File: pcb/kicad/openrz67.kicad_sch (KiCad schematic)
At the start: 58 parts, among them J1 GPIO header, U1 ESP32-C3FH4, U2 TPS63031DSKR, U3 BQ25185DLHR, U4 S4B-XH-A(LF)(SN), U5 TLP172AM, U6 TLP172AM, X1 40MHz, X2 32.768kHz

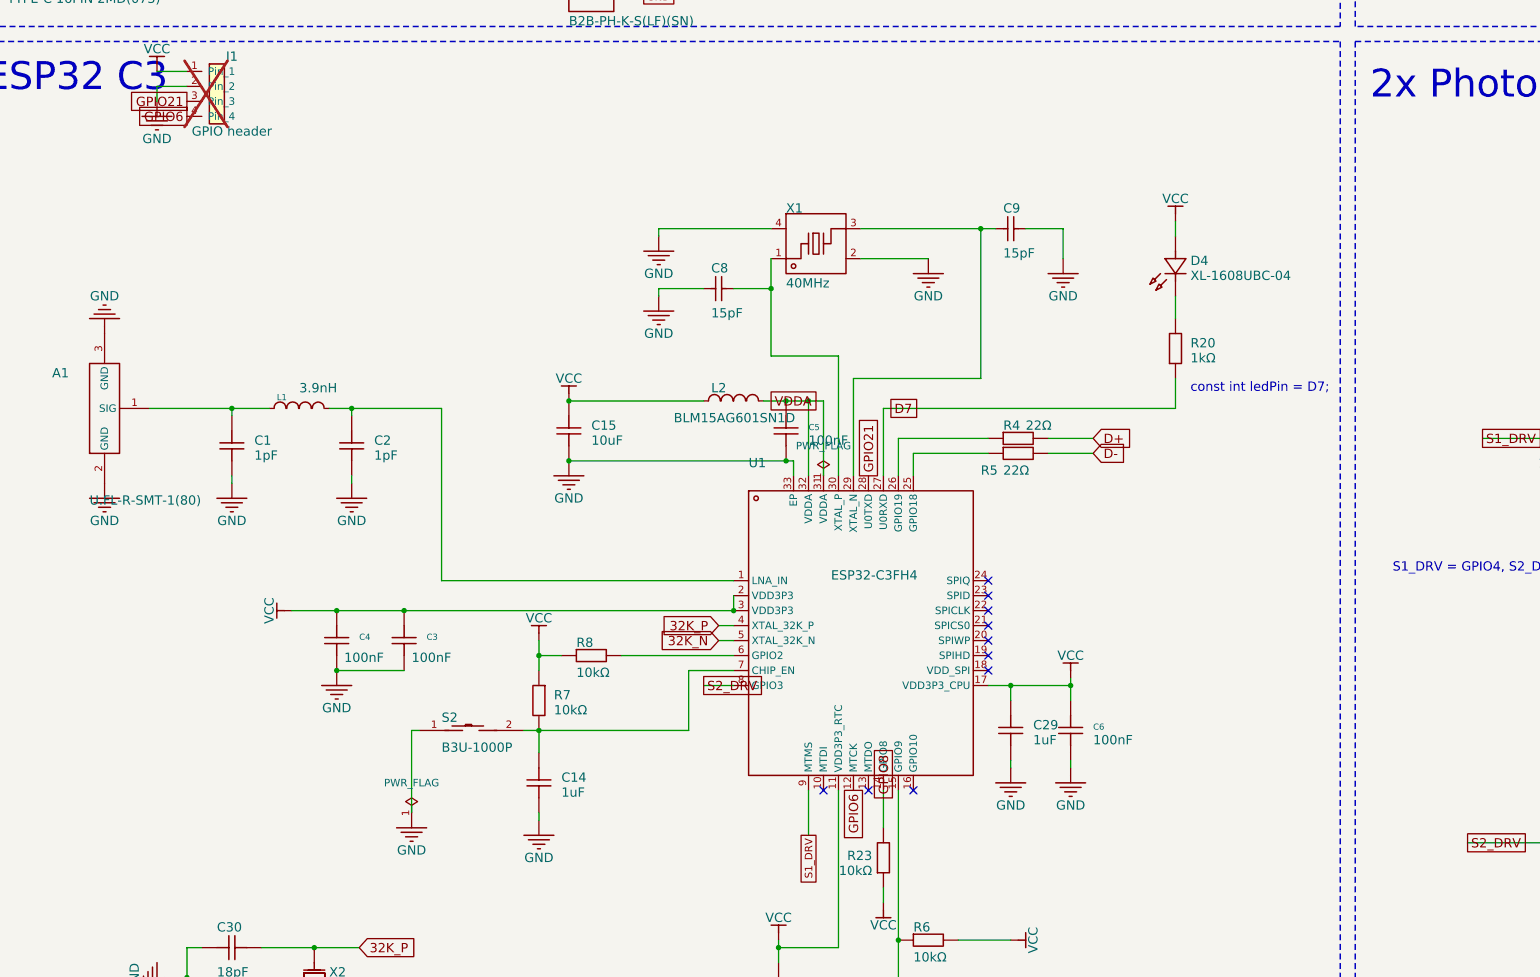
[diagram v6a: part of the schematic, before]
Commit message: PCB rev 3: battery voltage sense on GPIO3, S2 relay moved to GPIO6
R24/R25 1 MΩ + C32 100 nF under S3 divide SW_SYS (switched cell voltage; BQ25185
SYS voltage on USB) into GPIO3/ADC1_CH3 through the old S2_DRV copper. S2_DRV now
comes from GPIO6 (pin 12), fed off the existing GPIO6 track at (150.55, 99.3), so
J1 pin 4 carries the S2 drive. Every other spare pin was boxed in; BAT+ was
unreachable from U1. DRC 0 errors / 0 unconnected (two new courtyard warnings),
ERC unchanged, title block rev 3. Firmware todo for rev 3 in pcb/kicad/README.md;
src/ still targets rev 2.
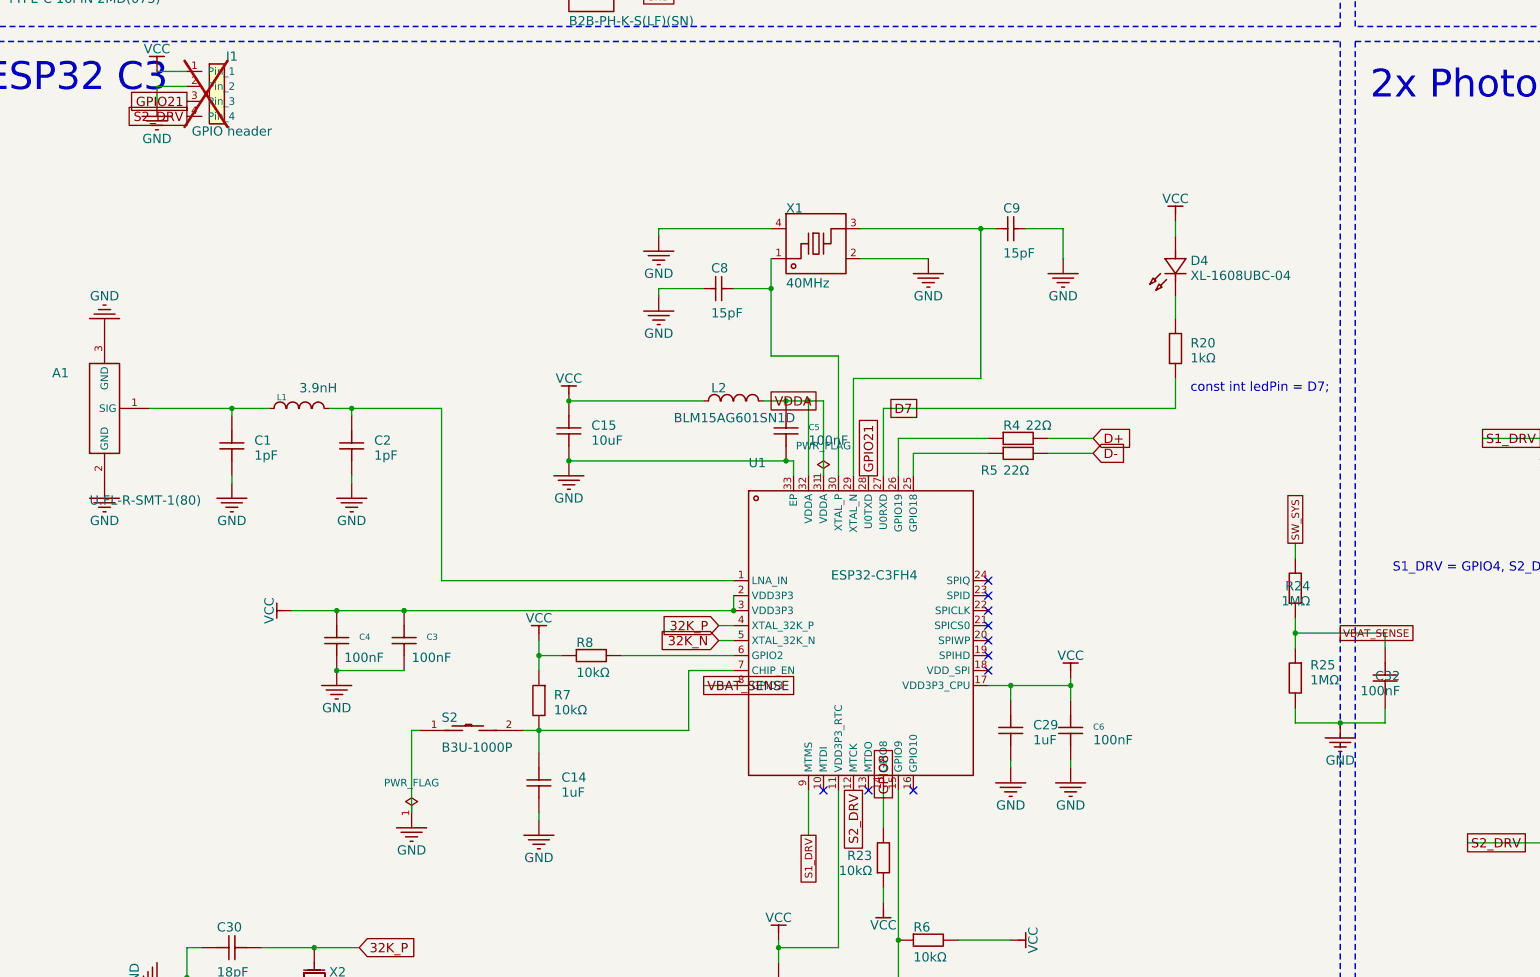
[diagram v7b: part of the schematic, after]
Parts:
- added C32: 100nF, openrz67:C0402, symbol openrz67:GRM155R71H104KE14D
- added R24, R25: 1MΩ, openrz67:R0402, symbol openrz67:0402WGF1004TCE
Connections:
- net GPIO6 is gone; now on net S2_DRV: J1.4 (Pin_4), U1.12 (MTCK)
- net GND: now also C32.1, R25.2
- net S2_DRV: no longer U1.8 (GPIO3)
- net SW_SYS: now also R24.2
- new net VBAT_SENSE: C32.2, R24.1, R25.1, U1.8 (GPIO3)
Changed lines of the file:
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@@
   (title_block
     (title "OpenRZ67 camera trigger")
-    (date "2026-09-03")
-    (rev "2")
+    (date "2026-09-15")
+    (rev "3")
     (comment 1 "Ported from EasyEDA Pro project ESP32C3CameraTrigger 2026-09-02 (rev with side-entry U4)")
   )
@@
     (effects (font (size 1.5748 1.5748)) (justify left bottom))
   )
-  (global_label "S2_DRV" (shape passive) (at 128.27 189.23 0)
+  (global_label "VBAT_SENSE" (shape passive) (at 128.27 189.23 0)
     (effects (font (size 1.5748 1.5748)) (justify left bottom))
   )
@@
     (effects (font (size 1.5748 1.5748)) (justify left bottom))
   )
-  (global_label "GPIO6" (shape passive) (at 40.64 92.71 180)
+  (global_label "S2_DRV" (shape passive) (at 40.64 92.71 180)
     (effects (font (size 1.5748 1.5748)) (justify right bottom))
   )
-  (global_label "GPIO6" (shape passive) (at 153.67 207.01 270)
+  (global_label "S2_DRV" (shape passive) (at 153.67 207.01 270)
     (effects (font (size 1.5748 1.5748)) (justify right bottom))
   )
@@
     (effects (font (size 1.27 1.27)) (justify left bottom))
   )
+  (global_label "SW_SYS" (shape passive) (at 228.6 165.1 90)
+    (effects (font (size 1.27 1.27)) (justify left bottom))
+  )
+  (wire (pts (xy 228.6 165.1) (xy 228.6 167.64))
+    (stroke (width 0) (type default))
+  )
+  (symbol (lib_id "openrz67:0402WGF1004TCE") (at 228.6 172.72 90) (unit 1)
+    (in_bom yes) (on_board yes) (dnp no)
+    (property "Reference" "R24" (at 231.14 171.45 90)
+      (effects (font (size 1.5748 1.5748)) (justify left bottom))
+    )
+    (property "Value" "1MΩ" (at 231.14 173.99 90)
+      (effects (font (size 1.5748 1.5748)) (justify left bottom))
+    )
+    (property "Footprint" "openrz67:R0402" (at 228.6 172.72 0)
+      (effects (font (size 1.27 1.27)) hide)
+    )
+    (property "Datasheet" "https://www.lcsc.com/product-detail/C26083.html" (at 228.6 172.72 0)
+      (effects (font (size 1.27 1.27)) hide)
+    )
+    (property "Description" "" (at 228.6 172.72 0)
+      (effects (font (size 1.27 1.27)) hide)
+    )
+    (property "Manufacturer Part" "0402WGF1004TCE" (at 228.6 172.72 0)
+      (effects (font (size 1.27 1.27)) hide)
+    )
+    (property "Manufacturer" "UNI-ROYAL(厚声)" (at 228.6 172.72 0)
+      (effects (font (size 1.27 1.27)) hide)
+    )
+    (property "Supplier Part" "C26083" (at 228.6 172.72 0)
+      (effects (font (size 1.27 1.27)) hide)
+    )
+    (property "Supplier" "LCSC" (at 228.6 172.72 0)
+      (effects (font (size 1.27 1.27)) hide)
+    )
+    (property "LCSC Part Name" "1MΩ ±1% 62.5mW 厚膜电阻" (at 228.6 172.72 0)
+      (effects (font (size 1.27 1.27)) hide)
+    )
+    (pin "1")
+    (pin "2")
+    (instances
+      (project "openrz67"
+        (path "/608428cc-ede5-4359-a9e7-0ca7713b40fb"
+          (reference "R24") (unit 1)
+        )
+      )
+    )
+  )
+  (wire (pts (xy 228.6 177.8) (xy 228.6 180.34))
+    (stroke (width 0) (type default))
+  )
+  (wire (pts (xy 228.6 180.34) (xy 228.6 182.88))
+    (stroke (width 0) (type default))
+  )
+  (junction (at 228.6 180.34) (diameter 0) (color 0 0 0 0)
+  )
+  (wire (pts (xy 228.6 180.34) (xy 243.84 180.34))
+    (stroke (width 0) (type default))
+  )
+  (wire (pts (xy 243.84 180.34) (xy 243.84 182.88))
+    (stroke (width 0) (type default))
+  )
+  (global_label "VBAT_SENSE" (shape passive) (at 236.22 180.34 0)
+    (effects (font (size 1.27 1.27)) (justify left bottom))
+  )
+  (symbol (lib_id "openrz67:0402WGF1004TCE") (at 228.6 187.96 270) (unit 1)
+    (in_bom yes) (on_board yes) (dnp no)
+    (property "Reference" "R25" (at 231.14 186.69 90)
+      (effects (font (size 1.5748 1.5748)) (justify left bottom))
+    )
+    (property "Value" "1MΩ" (at 231.14 189.23000000000002 90)
+      (effects (font (size 1.5748 1.5748)) (justify left bottom))
+    )
+    (property "Footprint" "openrz67:R0402" (at 228.6 187.96 0)
+      (effects (font (size 1.27 1.27)) hide)
+    )
+    (property "Datasheet" "https://www.lcsc.com/product-detail/C26083.html" (at 228.6 187.96 0)
+      (effects (font (size 1.27 1.27)) hide)
+    )
+    (property "Description" "" (at 228.6 187.96 0)
+      (effects (font (size 1.27 1.27)) hide)
+    )
+    (property "Manufacturer Part" "0402WGF1004TCE" (at 228.6 187.96 0)
+      (effects (font (size 1.27 1.27)) hide)
+    )
+    (property "Manufacturer" "UNI-ROYAL(厚声)" (at 228.6 187.96 0)
+      (effects (font (size 1.27 1.27)) hide)
+    )
+    (property "Supplier Part" "C26083" (at 228.6 187.96 0)
+      (effects (font (size 1.27 1.27)) hide)
+    )
+    (property "Supplier" "LCSC" (at 228.6 187.96 0)
+      (effects (font (size 1.27 1.27)) hide)
+    )
+    (property "LCSC Part Name" "1MΩ ±1% 62.5mW 厚膜电阻" (at 228.6 187.96 0)
+      (effects (font (size 1.27 1.27)) hide)
+    )
+    (pin "1")
+    (pin "2")
+    (instances
+      (project "openrz67"
+        (path "/608428cc-ede5-4359-a9e7-0ca7713b40fb"
+          (reference "R25") (unit 1)
+        )
+      )
+    )
+  )
+  (symbol (lib_id "openrz67:GRM155R71H104KE14D") (at 243.84 187.96 90) (unit 1)
+    (in_bom yes) (on_board yes) (dnp no)
+    (property "Reference" "C32" (at 246.38 186.69 90)
+      (effects (font (size 1.5748 1.5748)) (justify left bottom))
+    )
+    (property "Value" "100nF" (at 246.38 189.23000000000002 90)
+      (effects (font (size 1.5748 1.5748)) (justify left bottom))
+    )
+    (property "Footprint" "openrz67:C0402" (at 243.84 187.96 0)
+      (effects (font (size 1.27 1.27)) hide)
+    )
+    (property "Datasheet" "https://atta.szlcsc.com/upload/public/pdf/source/20180326/C77020_39BD49C951FF1AF0DB1F1FAC5AC1E401.pdf" (at 243.84 187.96 0)
+      (effects (font (size 1.27 1.27)) hide)
+    )
+    (property "Description" "battery sense filter" (at 243.84 187.96 0)
+      (effects (font (size 1.27 1.27)) hide)
+    )
+    (property "Manufacturer Part" "GRM155R71H104KE14D" (at 243.84 187.96 0)
+      (effects (font (size 1.27 1.27)) hide)
+    )
+    (property "Manufacturer" "muRata(村田)" (at 243.84 187.96 0)
+      (effects (font (size 1.27 1.27)) hide)
+    )
+    (property "Supplier Part" "C77020" (at 243.84 187.96 0)
+      (effects (font (size 1.27 1.27)) hide)
+    )
+    (property "Supplier" "LCSC" (at 243.84 187.96 0)
+      (effects (font (size 1.27 1.27)) hide)
+    )
+    (property "LCSC Part Name" "100nF ±10% 50V" (at 243.84 187.96 0)
+      (effects (font (size 1.27 1.27)) hide)
+    )
+    (pin "1")
+    (pin "2")
+    (instances
+      (project "openrz67"
+        (path "/608428cc-ede5-4359-a9e7-0ca7713b40fb"
+          (reference "C32") (unit 1)
+        )
+      )
+    )
+  )
+  (wire (pts (xy 228.6 193.04) (xy 228.6 195.58))
+    (stroke (width 0) (type default))
+  )
+  (wire (pts (xy 243.84 193.04) (xy 243.84 195.58))
+    (stroke (width 0) (type default))
+  )
+  (wire (pts (xy 228.6 195.58) (xy 236.22 195.58))
+    (stroke (width 0) (type default))
+  )
+  (wire (pts (xy 236.22 195.58) (xy 243.84 195.58))
+    (stroke (width 0) (type default))
+  )
+  (junction (at 236.22 195.58) (diameter 0) (color 0 0 0 0)
+  )
+  (symbol (lib_id "openrz67:Ground-GND") (at 236.22 195.58 0) (unit 1)
+    (in_bom yes) (on_board yes) (dnp no)
+    (property "Reference" "#PWR066" (at 236.22 195.58 0)
+      (effects (font (size 1.27 1.27)) hide)
+    )
+    (property "Value" "GND" (at 236.22 201.93 0)
+      (effects (font (size 1.5748 1.5748)))
+    )
+    (property "Footprint" "" (at 236.22 195.58 0)
+      (effects (font (size 1.27 1.27)) hide)
+    )
+    (property "Datasheet" "" (at 236.22 195.58 0)
+      (effects (font (size 1.27 1.27)) hide)
+    )
+    (property "Description" "" (at 236.22 195.58 0)
+      (effects (font (size 1.27 1.27)) hide)
+    )
+    (pin "1")
+    (instances
+      (project "openrz67"
+        (path "/608428cc-ede5-4359-a9e7-0ca7713b40fb"
+          (reference "#PWR066") (unit 1)
+        )
+      )
+    )
+  )
   (symbol (lib_id "openrz67:XKXGI-SUA-32.768K") (at 62.23 238.76 90) (unit 1)

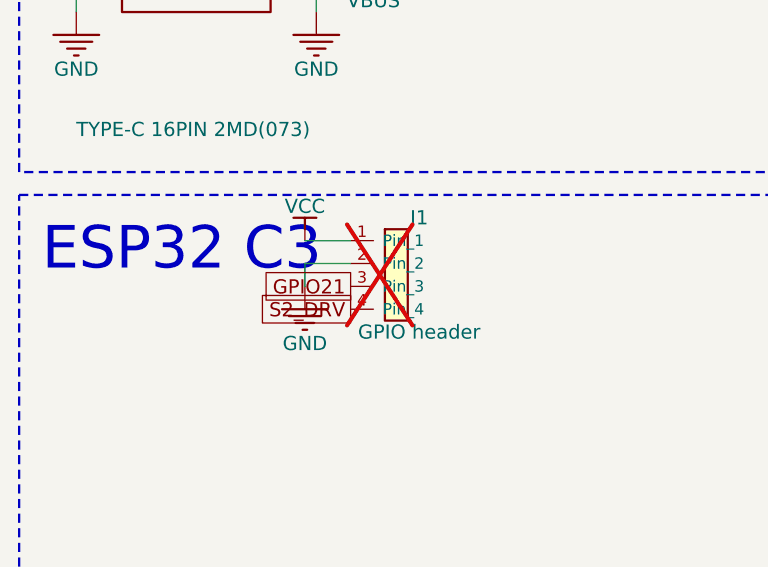
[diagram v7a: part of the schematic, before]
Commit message: PCB rev 3: J1 shrinks to 1x3 (3V3, GND, TX); GPIO6 track to the old pin 4 and IO6 silk removed
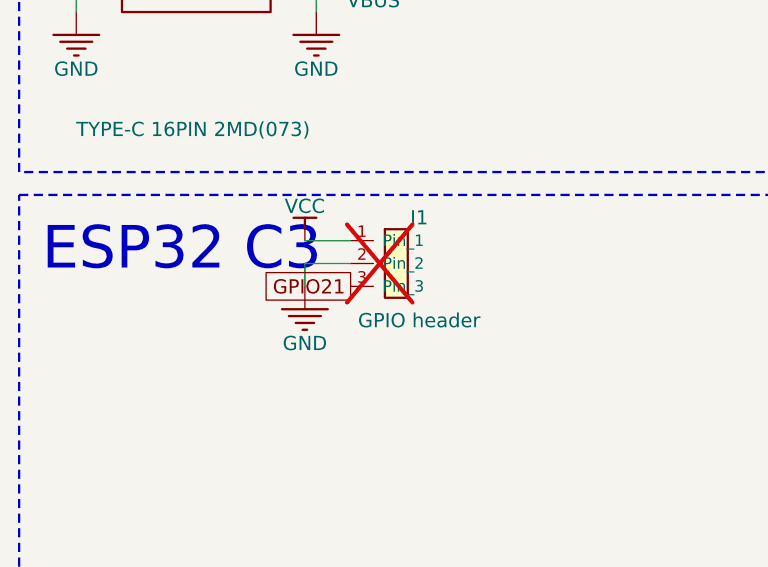
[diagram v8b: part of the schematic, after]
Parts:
- J1: footprint openrz67:PinHeader_1x04_P2.54mm_Vertical -> openrz67:PinHeader_1x03_P2.54mm_Vertical; symbol openrz67:Conn_01x04 -> openrz67:Conn_01x03
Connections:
- net S2_DRV: no longer J1.4 (Pin_4)
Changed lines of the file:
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@@
     (effects (font (size 1.5748 1.5748)) (justify left bottom))
   )
-  (global_label "S2_DRV" (shape passive) (at 40.64 92.71 180)
-    (effects (font (size 1.5748 1.5748)) (justify right bottom))
-  )
   (global_label "S2_DRV" (shape passive) (at 153.67 207.01 270)
     (effects (font (size 1.5748 1.5748)) (justify right bottom))
@@
     )
   )
-  (symbol (lib_id "openrz67:Conn_01x04") (at 45.72 88.9 0) (unit 1)
+  (symbol (lib_id "openrz67:Conn_01x03") (at 45.72 87.63 0) (unit 1)
     (in_bom no) (on_board yes) (dnp yes)
     (property "Reference" "J1" (at 48.26 82.55 0)
       (effects (font (size 1.5748 1.5748)))
     )
-    (property "Value" "GPIO header" (at 48.26 95.25 0)
+    (property "Value" "GPIO header" (at 48.26 93.98 0)
       (effects (font (size 1.5748 1.5748)))
     )
-    (property "Footprint" "openrz67:PinHeader_1x04_P2.54mm_Vertical" (at 45.72 88.9 0)
+    (property "Footprint" "openrz67:PinHeader_1x03_P2.54mm_Vertical" (at 45.72 87.63 0)
       (effects (font (size 1.27 1.27)) hide)
     )
-    (property "Datasheet" "" (at 45.72 88.9 0)
+    (property "Datasheet" "" (at 45.72 87.63 0)
       (effects (font (size 1.27 1.27)) hide)
     )
-    (property "Description" "1x4 2.54 mm pin header, not populated by the assembler" (at 45.72 88.9 0)
+    (property "Description" "1x3 2.54 mm pin header, not populated by the assembler" (at 45.72 87.63 0)
       (effects (font (size 1.27 1.27)) hide)
     )
@@
     (pin "2")
     (pin "3")
-    (pin "4")
     (instances
       (project "openrz67"
